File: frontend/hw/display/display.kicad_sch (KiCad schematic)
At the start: 15 parts, among them J1 Conn_01x04, J2 Conn_02x17_Odd_Even, Q1 MMBT3904, Q2 MMBT3904, U1 ESP32-WROOM-32U, U2 CH340C, U3 AMS1117-3.3

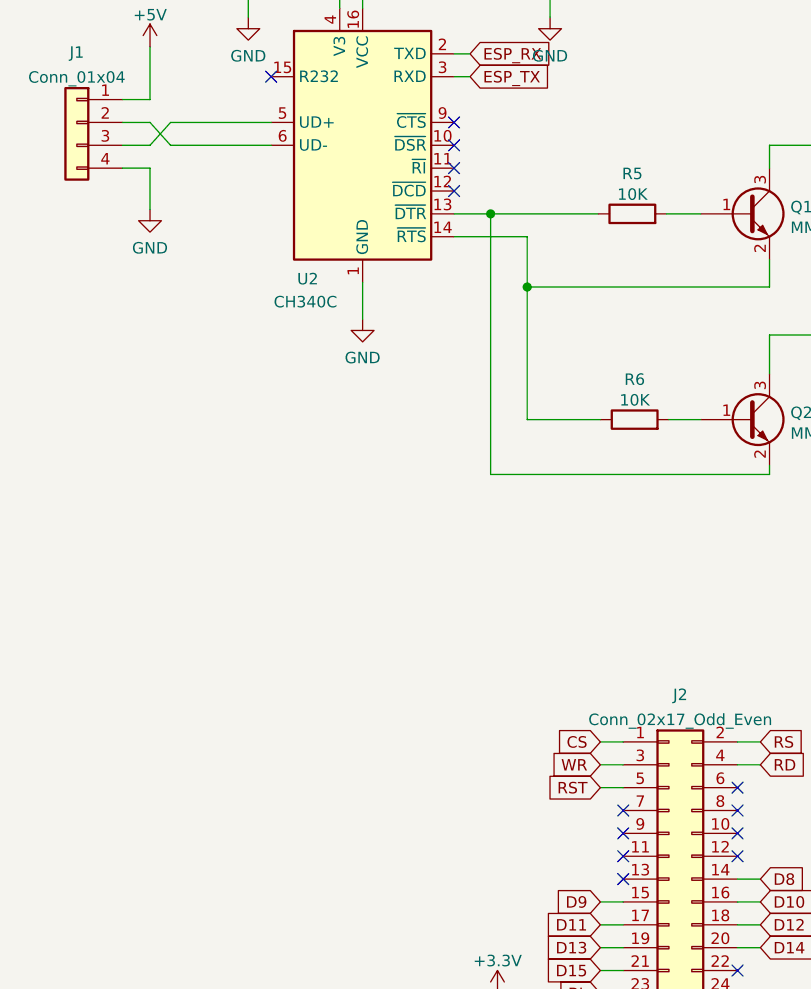
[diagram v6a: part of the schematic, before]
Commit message: Add boot switch.
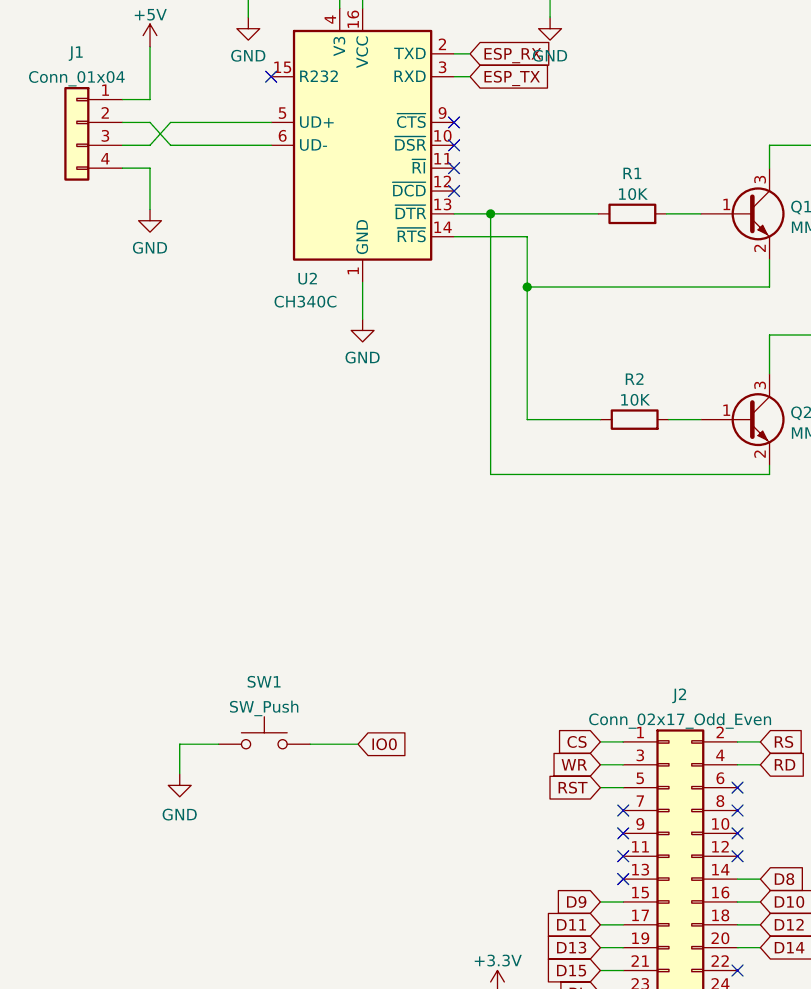
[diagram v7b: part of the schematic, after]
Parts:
- added SW1: SW_Push, Button_Switch_SMD:SW_Push_SPST_NO_Alps_SKRK, symbol Switch:SW_Push
- renumbered R5 to R1, R6 to R2
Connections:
- net GND: now also SW1.1
- net IO0: now also SW1.2
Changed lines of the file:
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@@
     (stroke (width 0) (type solid) (color 0 0 0 0))
+  )
+  (wire (pts (xy 35.56 135.89) (xy 35.56 132.588))
+    (stroke (width 0) (type default) (color 0 0 0 0))
   )
   (wire (pts (xy 82.296 170.434) (xy 84.836 170.434))
@@
     (stroke (width 0) (type default) (color 0 0 0 0))
   )
+  (wire (pts (xy 50.038 132.588) (xy 55.372 132.588))
+    (stroke (width 0) (type default) (color 0 0 0 0))
+  )
   (wire (pts (xy 171.45 61.976) (xy 177.546 61.976))
     (stroke (width 0) (type solid) (color 0 0 0 0))
@@
   )
   (wire (pts (xy 110.49 157.734) (xy 110.49 160.274))
+    (stroke (width 0) (type default) (color 0 0 0 0))
+  )
+  (wire (pts (xy 35.56 132.588) (xy 39.878 132.588))
     (stroke (width 0) (type default) (color 0 0 0 0))
   )
@@
     )
   )
+  (global_label "IO0" (shape input) (at 55.372 132.588 0) (fields_autoplaced)
+    (effects (font (size 1.27 1.27)) (justify left))
+    (property "Intersheet References" "${INTERSHEET_REFS}" (id 0) (at 61.1204 132.5086 0)
+      (effects (font (size 1.27 1.27)) (justify left) hide)
+    )
+  )
   (global_label "CS" (shape input) (at 82.296 132.334 180) (fields_autoplaced)
     (effects (font (size 1.27 1.27)) (justify right))
@@
   (symbol (lib_id "Device:R") (at 86.106 96.52 90) (unit 1)
     (in_bom yes) (on_board yes) (fields_autoplaced)
-    (property "Reference" "R6" (id 0) (at 86.106 92.0708 90))
+    (property "Reference" "R2" (id 0) (at 86.106 92.0708 90))
     (property "Value" "10K" (id 1) (at 86.106 94.3695 90))
     (property "Footprint" "Resistor_SMD:R_0603_1608Metric" (id 2) (at 86.106 98.298 90)
@@
     (pin "1")
   )
+  (symbol (lib_id "Switch:SW_Push") (at 44.958 132.588 0) (unit 1)
+    (in_bom yes) (on_board yes) (fields_autoplaced)
+    (property "Reference" "SW1" (id 0) (at 44.958 125.7005 0))
+    (property "Value" "SW_Push" (id 1) (at 44.958 128.4756 0))
+    (property "Footprint" "Button_Switch_SMD:SW_Push_SPST_NO_Alps_SKRK" (id 2) (at 44.958 127.508 0)
+      (effects (font (size 1.27 1.27)) hide)
+    )
+    (property "Datasheet" "~" (id 3) (at 44.958 127.508 0)
+      (effects (font (size 1.27 1.27)) hide)
+    )
+    (pin "1")
+    (pin "2")
+  )
   (symbol (lib_id "power:+5V") (at 214.376 136.144 0) (unit 1)
     (in_bom yes) (on_board yes) (fields_autoplaced)
@@
   (symbol (lib_id "Device:R") (at 85.852 73.66 90) (unit 1)
     (in_bom yes) (on_board yes) (fields_autoplaced)
-    (property "Reference" "R5" (id 0) (at 85.852 69.2108 90))
+    (property "Reference" "R1" (id 0) (at 85.852 69.2108 90))
     (property "Value" "10K" (id 1) (at 85.852 71.5095 90))
     (property "Footprint" "Resistor_SMD:R_0603_1608Metric" (id 2) (at 85.852 75.438 90)
@@
     (pin "1")
   )
+  (symbol (lib_id "power:GND") (at 35.56 135.89 0) (unit 1)
+    (in_bom yes) (on_board yes) (fields_autoplaced)
+    (property "Reference" "#PWR01" (id 0) (at 35.56 142.24 0)
+      (effects (font (size 1.27 1.27)) hide)
+    )
+    (property "Value" "GND" (id 1) (at 35.56 140.4525 0))
+    (property "Footprint" "" (id 2) (at 35.56 135.89 0)
+      (effects (font (size 1.27 1.27)) hide)
+    )
+    (property "Datasheet" "" (id 3) (at 35.56 135.89 0)
+      (effects (font (size 1.27 1.27)) hide)
+    )
+    (pin "1")
+  )
   (symbol (lib_id "power:GND") (at 174.498 44.45 0) (unit 1)
     (in_bom yes) (on_board yes) (fields_autoplaced)
@@
       (reference "#FLG0101") (unit 1) (value "PWR_FLAG") (footprint "")
     )
+    (path "/af5b0949-f220-41df-9675-e4adeb75ceb0"
+      (reference "#PWR01") (unit 1) (value "GND") (footprint "")
+    )
     (path "/f3787df9-6344-42f0-b474-f781ef32cc09"
       (reference "#PWR06") (unit 1) (value "GND") (footprint "")
@@
     )
     (path "/50a5b604-8542-4f2b-a8ad-b7af9739f848"
-      (reference "R5") (unit 1) (value "10K") (footprint "Resistor_SMD:R_0603_1608Metric")
+      (reference "R1") (unit 1) (value "10K") (footprint "Resistor_SMD:R_0603_1608Metric")
     )
     (path "/055e2db9-ea27-443d-9535-2f3050b668ec"
-      (reference "R6") (unit 1) (value "10K") (footprint "Resistor_SMD:R_0603_1608Metric")
+      (reference "R2") (unit 1) (value "10K") (footprint "Resistor_SMD:R_0603_1608Metric")
+    )
+    (path "/11316c6e-c6b6-4377-9342-a7648e7f77be"
+      (reference "SW1") (unit 1) (value "SW_Push") (footprint "Button_Switch_SMD:SW_Push_SPST_NO_Alps_SKRK")
     )
     (path "/647440a9-0aaf-4b33-9087-36e43e3aa36f"
